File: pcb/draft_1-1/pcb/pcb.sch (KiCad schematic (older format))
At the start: 24 parts, among them J1 USB4110-GF-A, U1 H3LIS200DLTR, U2 ATSAML21J16B-AUT, U3 BQ25155

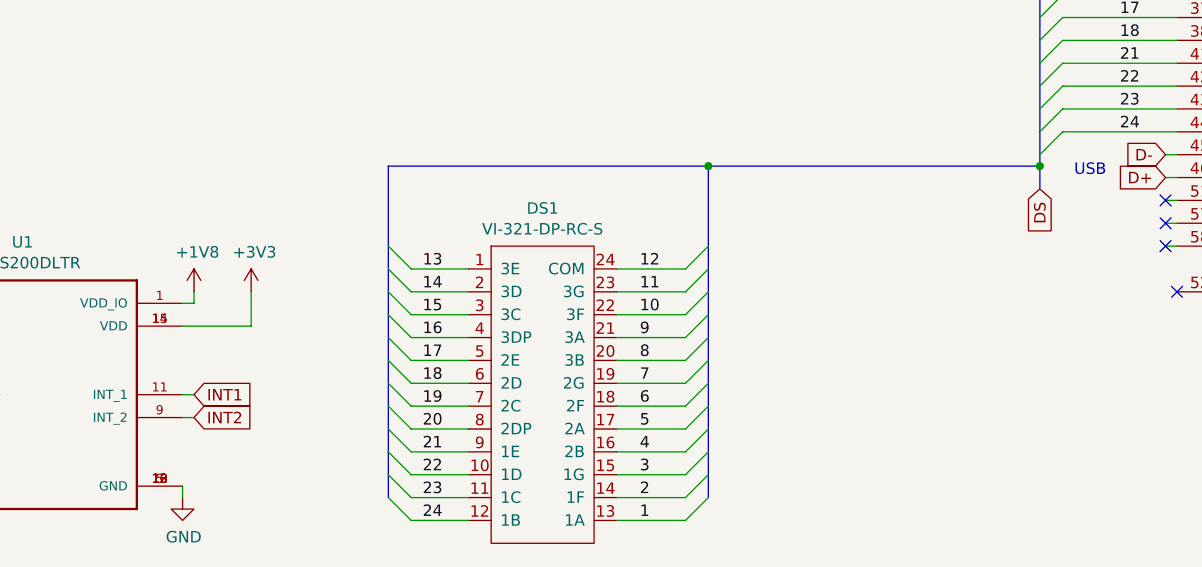
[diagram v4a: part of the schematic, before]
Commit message: added accel decouple caps
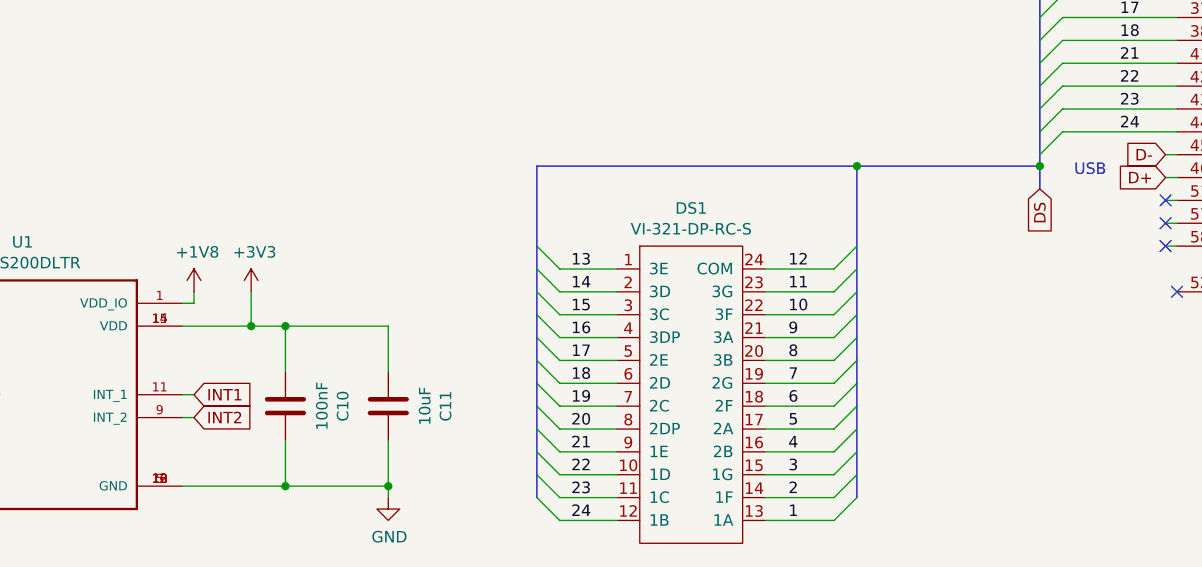
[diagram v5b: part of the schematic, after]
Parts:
- added C10: 100nF, Capacitor_SMD:C_0402_1005Metric, symbol Device:C
- added C11: 10uF, Capacitor_SMD:C_0805_2012Metric, symbol Device:C
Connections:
- net +1V8: now also C10.2, C11.2
- net GND: now also C10.1, C11.1
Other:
- moved on the sheet: DS1
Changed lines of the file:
@@
 $EndComp
 Entry Wire Line
-	4350 5300 4450 5400
-Text Label 4500 5400 0    50   ~ 0
+	5000 5300 5100 5400
+Text Label 5150 5400 0    50   ~ 0
 13
 Entry Wire Line
-	4350 5400 4450 5500
-Entry Wire Line
-	4350 5500 4450 5600
-Entry Wire Line
-	4350 5600 4450 5700
-Entry Wire Line
-	4350 5700 4450 5800
-Entry Wire Line
-	4350 5800 4450 5900
-Entry Wire Line
-	4350 6000 4450 6100
-Entry Wire Line
-	4350 5900 4450 6000
-Entry Wire Line
-	4350 6100 4450 6200
-Entry Wire Line
-	4350 6200 4450 6300
-Entry Wire Line
-	4350 6300 4450 6400
-Entry Wire Line
-	4350 6400 4450 6500
-Text Label 4500 5500 0    50   ~ 0
+	5000 5400 5100 5500
+Entry Wire Line
+	5000 5500 5100 5600
+Entry Wire Line
+	5000 5600 5100 5700
+Entry Wire Line
+	5000 5700 5100 5800
+Entry Wire Line
+	5000 5800 5100 5900
+Entry Wire Line
+	5000 6000 5100 6100
+Entry Wire Line
+	5000 5900 5100 6000
+Entry Wire Line
+	5000 6100 5100 6200
+Entry Wire Line
+	5000 6200 5100 6300
+Entry Wire Line
+	5000 6300 5100 6400
+Entry Wire Line
+	5000 6400 5100 6500
+Text Label 5150 5500 0    50   ~ 0
 14
-Text Label 4500 5600 0    50   ~ 0
+Text Label 5150 5600 0    50   ~ 0
 15
-Text Label 4500 5700 0    50   ~ 0
+Text Label 5150 5700 0    50   ~ 0
 16
-Text Label 4500 5800 0    50   ~ 0
+Text Label 5150 5800 0    50   ~ 0
 17
-Text Label 4500 5900 0    50   ~ 0
+Text Label 5150 5900 0    50   ~ 0
 18
-Text Label 4500 6000 0    50   ~ 0
+Text Label 5150 6000 0    50   ~ 0
 19
-Text Label 4500 6100 0    50   ~ 0
+Text Label 5150 6100 0    50   ~ 0
 20
-Text Label 4500 6200 0    50   ~ 0
+Text Label 5150 6200 0    50   ~ 0
 21
-Text Label 4500 6300 0    50   ~ 0
+Text Label 5150 6300 0    50   ~ 0
 22
-Text Label 4500 6400 0    50   ~ 0
+Text Label 5150 6400 0    50   ~ 0
 23
-Text Label 4500 6500 0    50   ~ 0
+Text Label 5150 6500 0    50   ~ 0
 24
 Entry Wire Line
-	5650 5400 5750 5300
-Entry Wire Line
-	5650 5500 5750 5400
-Entry Wire Line
-	5650 5600 5750 5500
-Entry Wire Line
-	5650 5700 5750 5600
-Entry Wire Line
-	5650 5800 5750 5700
-Entry Wire Line
-	5650 5900 5750 5800
-Entry Wire Line
-	5650 6000 5750 5900
-Entry Wire Line
-	5650 6100 5750 6000
-Entry Wire Line
-	5650 6200 5750 6100
-Entry Wire Line
-	5650 6300 5750 6200
-Entry Wire Line
-	5650 6400 5750 6300
-Entry Wire Line
-	5650 6500 5750 6400
-Text Label 5450 5400 0    50   ~ 0
+	6300 5400 6400 5300
+Entry Wire Line
+	6300 5500 6400 5400
+Entry Wire Line
+	6300 5600 6400 5500
+Entry Wire Line
+	6300 5700 6400 5600
+Entry Wire Line
+	6300 5800 6400 5700
+Entry Wire Line
+	6300 5900 6400 5800
+Entry Wire Line
+	6300 6000 6400 5900
+Entry Wire Line
+	6300 6100 6400 6000
+Entry Wire Line
+	6300 6200 6400 6100
+Entry Wire Line
+	6300 6300 6400 6200
+Entry Wire Line
+	6300 6400 6400 6300
+Entry Wire Line
+	6300 6500 6400 6400
+Text Label 6100 5400 0    50   ~ 0
 12
-Text Label 5450 5500 0    50   ~ 0
+Text Label 6100 5500 0    50   ~ 0
 11
-Text Label 5450 5600 0    50   ~ 0
+Text Label 6100 5600 0    50   ~ 0
 10
-Text Label 5450 5700 0    50   ~ 0
+Text Label 6100 5700 0    50   ~ 0
 9
-Text Label 5450 5800 0    50   ~ 0
+Text Label 6100 5800 0    50   ~ 0
 8
-Text Label 5450 5900 0    50   ~ 0
+Text Label 6100 5900 0    50   ~ 0
 7
-Text Label 5450 6000 0    50   ~ 0
+Text Label 6100 6000 0    50   ~ 0
 6
-Text Label 5450 6100 0    50   ~ 0
+Text Label 6100 6100 0    50   ~ 0
 5
-Text Label 5450 6200 0    50   ~ 0
+Text Label 6100 6200 0    50   ~ 0
 4
-Text Label 5450 6300 0    50   ~ 0
+Text Label 6100 6300 0    50   ~ 0
 3
-Text Label 5450 6400 0    50   ~ 0
+Text Label 6100 6400 0    50   ~ 0
 2
-Text Label 5450 6500 0    50   ~ 0
+Text Label 6100 6500 0    50   ~ 0
 1
 Text GLabel 1150 5950 0    50   Input ~ 0
@@
 L power:GND #PWR0102
 U 1 1 5E0D1684
-P 3450 6400
-F 0 "#PWR0102" H 3450 6150 50  0001 C CNN
-F 1 "GND" H 3455 6227 50  0000 C CNN
-F 2 "" H 3450 6400 50  0001 C CNN
-F 3 "" H 3450 6400 50  0001 C CNN
-	1    3450 6400
-	1    0    0    -1
-$EndComp
-Wire Wire Line
-	3450 6350 3450 6400
+P 4350 6400
+F 0 "#PWR0102" H 4350 6150 50  0001 C CNN
+F 1 "GND" H 4355 6227 50  0000 C CNN
+F 2 "" H 4350 6400 50  0001 C CNN
+F 3 "" H 4350 6400 50  0001 C CNN
+	1    4350 6400
+	1    0    0    -1
+$EndComp
 $Comp
 L power:+1V8 #PWR0103
@@
 	1    0    0    -1
 $EndComp
-Text GLabel 3500 5950 2    50   Input ~ 0
-INT1
 Text GLabel 3500 6050 2    50   Input ~ 0
 INT2
@@
 L Custom:VI-321-DP-RC-S DS1
 U 1 1 5E20A245
-P 5050 5950
-F 0 "DS1" H 5025 6765 50  0000 C CNN
-F 1 "VI-321-DP-RC-S" H 5025 6674 50  0000 C CNN
-F 2 "custom:VI-321-DP-RC-S" H 5250 6350 50  0001 C CNN
-F 3 "" H 5250 6350 50  0001 C CNN
-	1    5050 5950
+P 5700 5950
+F 0 "DS1" H 5675 6765 50  0000 C CNN
+F 1 "VI-321-DP-RC-S" H 5675 6674 50  0000 C CNN
+F 2 "custom:VI-321-DP-RC-S" H 5900 6350 50  0001 C CNN
+F 3 "" H 5900 6350 50  0001 C CNN
+	1    5700 5950
 	1    0    0    -1
 $EndComp
@@
 	7300 4800 7800 4800
 Wire Wire Line
-	5350 5400 5650 5400
-Wire Wire Line
-	5350 5500 5650 5500
-Wire Wire Line
-	5350 5600 5650 5600
-Wire Wire Line
-	5350 5700 5650 5700
-Wire Wire Line
-	5350 5800 5650 5800
-Wire Wire Line
-	5350 5900 5650 5900
-Wire Wire Line
-	5350 6000 5650 6000
-Wire Wire Line
-	5350 6100 5650 6100
-Wire Wire Line
-	5350 6200 5650 6200
-Wire Wire Line
-	5350 6300 5650 6300
-Wire Wire Line
-	5350 6400 5650 6400
-Wire Wire Line
-	5350 6500 5650 6500
-Wire Wire Line
-	4450 5400 4700 5400
-Wire Wire Line
-	4450 5500 4700 5500
-Wire Wire Line
-	4450 5600 4700 5600
-Wire Wire Line
-	4450 5700 4700 5700
-Wire Wire Line
-	4450 5800 4700 5800
-Wire Wire Line
-	4450 5900 4700 5900
-Wire Wire Line
-	4450 6000 4700 6000
-Wire Wire Line
-	4450 6100 4700 6100
-Wire Wire Line
-	4450 6200 4700 6200
-Wire Wire Line
-	4450 6300 4700 6300
-Wire Wire Line
-	4450 6400 4700 6400
-Wire Wire Line
-	4450 6500 4700 6500
+	6000 5400 6300 5400
+Wire Wire Line
+	6000 5500 6300 5500
+Wire Wire Line
+	6000 5600 6300 5600
+Wire Wire Line
+	6000 5700 6300 5700
+Wire Wire Line
+	6000 5800 6300 5800
+Wire Wire Line
+	6000 5900 6300 5900
+Wire Wire Line
+	6000 6000 6300 6000
+Wire Wire Line
+	6000 6100 6300 6100
+Wire Wire Line
+	6000 6200 6300 6200
+Wire Wire Line
+	6000 6300 6300 6300
+Wire Wire Line
+	6000 6400 6300 6400
+Wire Wire Line
+	6000 6500 6300 6500
+Wire Wire Line
+	5100 5400 5350 5400
+Wire Wire Line
+	5100 5500 5350 5500
+Wire Wire Line
+	5100 5600 5350 5600
+Wire Wire Line
+	5100 5700 5350 5700
+Wire Wire Line
+	5100 5800 5350 5800
+Wire Wire Line
+	5100 5900 5350 5900
+Wire Wire Line
+	5100 6000 5350 6000
+Wire Wire Line
+	5100 6100 5350 6100
+Wire Wire Line
+	5100 6200 5350 6200
+Wire Wire Line
+	5100 6300 5350 6300
+Wire Wire Line
+	5100 6400 5350 6400
+Wire Wire Line
+	5100 6500 5350 6500
 Wire Bus Line
-	4350 4950 5750 4950
-Connection ~ 5750 4950
-Wire Bus Line
-	5750 4950 7200 4950
+	5000 4950 6400 4950
 Text GLabel 7200 5050 3    50   Input ~ 0
 DS
@@
 Text Label 7550 4500 0    50   ~ 0
 21
-Wire Bus Line
-	7200 5050 7200 4950
-Connection ~ 7200 4950
 Wire Wire Line
 	7500 3000 7800 3000
@@
 NoConn ~ 7750 5300
 NoConn ~ 7800 5500
-Wire Bus Line
-	10200 3700 10200 4500
-Wire Bus Line
-	4350 4950 4350 6400
-Wire Bus Line
-	5750 4950 5750 6400
-Wire Bus Line
-	7200 3400 7200 4950
 Text Label 7550 4400 0    50   ~ 0
 18
 Text Label 7550 4300 0    50   ~ 0
 17
+Wire Bus Line
+	6400 4950 7200 4950
+Connection ~ 6400 4950
+Connection ~ 7200 4950
+Wire Bus Line
+	7200 4950 7200 5050
+Wire Wire Line
+	3750 5650 3900 5650
+Connection ~ 3750 5650
+Wire Wire Line
+	3900 5650 4350 5650
+Connection ~ 3900 5650
+Wire Wire Line
+	3450 6350 3900 6350
+Wire Wire Line
+	4350 6350 4350 6400
+Connection ~ 4350 6350
+Connection ~ 3900 6350
+Wire Wire Line
+	3900 6350 4350 6350
+$Comp
+L Device:C C10
+U 1 1 5E17A014
+P 3900 6000
+F 0 "C10" V 3648 6000 50  0000 C CNN
+F 1 "100nF" V 3739 6000 50  0000 C CNN
+F 2 "Capacitor_SMD:C_0402_1005Metric" H 3938 5850 50  0001 C CNN
+F 3 "~" H 3900 6000 50  0001 C CNN
+	1    3900 6000
+	-1   0    0    1
+$EndComp
+$Comp
+L Device:C C11
+U 1 1 5E16FE35
+P 4350 6000
+F 0 "C11" V 4098 6000 50  0000 C CNN
+F 1 "10uF" V 4189 6000 50  0000 C CNN
+F 2 "Capacitor_SMD:C_0805_2012Metric" H 4388 5850 50  0001 C CNN
+F 3 "~" H 4350 6000 50  0001 C CNN
+	1    4350 6000
+	-1   0    0    1
+$EndComp
+Text GLabel 3500 5950 2    50   Input ~ 0
+INT1
+Wire Wire Line
+	3900 6150 3900 6350
+Wire Wire Line
+	4350 6150 4350 6350
+Wire Wire Line
+	3900 5650 3900 5850
+Wire Wire Line
+	4350 5650 4350 5850
+Wire Bus Line
+	10200 3700 10200 4500
+Wire Bus Line
+	5000 4950 5000 6400
+Wire Bus Line
+	6400 4950 6400 6400
+Wire Bus Line
+	7200 3400 7200 4950
 $EndSCHEMATC

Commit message: candidate layout done
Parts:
- C11: value 10uF -> 22uF
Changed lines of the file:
@@
 P 4350 6000
 F 0 "C11" V 4098 6000 50  0000 C CNN
-F 1 "10uF" V 4189 6000 50  0000 C CNN
+F 1 "22uF" V 4189 6000 50  0000 C CNN
 F 2 "Capacitor_SMD:C_0805_2012Metric" H 4388 5850 50  0001 C CNN
 F 3 "~" H 4350 6000 50  0001 C CNN

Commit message: as built
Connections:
- net 1 renamed 1A
- net 10 renamed 3F
- net 11 renamed 3G
- net 12 renamed COM
- net 13 renamed 3E
- net 14 renamed 3D
- net 15 renamed 3C
- net 16 renamed 3DP
- net 17 renamed 2E
- net 18 renamed 2D
- net 19 renamed 2C
- net 2 renamed 1F
- net 20 renamed 2DP
- net 21 renamed 1E
- net 22 renamed 1D
- net 23 renamed 1C
- net 24 renamed 1B
- net 3 renamed 1G
- net 4 renamed 2B
- net 5 renamed 2A
- net 6 renamed 2F
- net 7 renamed 2G
- net 8 renamed 3B
- net 9 renamed 3A
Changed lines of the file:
@@
 	5000 5300 5100 5400
 Text Label 5150 5400 0    50   ~ 0
-13
+3E
 Entry Wire Line
 	5000 5400 5100 5500
@@
 	5000 6400 5100 6500
 Text Label 5150 5500 0    50   ~ 0
-14
+3D
 Text Label 5150 5600 0    50   ~ 0
-15
+3C
 Text Label 5150 5700 0    50   ~ 0
-16
+3DP
 Text Label 5150 5800 0    50   ~ 0
-17
-Text Label 5150 5900 0    50   ~ 0
-18
+2E
 Text Label 5150 6000 0    50   ~ 0
-19
+2C
 Text Label 5150 6100 0    50   ~ 0
-20
+2DP
 Text Label 5150 6200 0    50   ~ 0
-21
+1E
 Text Label 5150 6300 0    50   ~ 0
-22
+1D
 Text Label 5150 6400 0    50   ~ 0
-23
+1C
 Text Label 5150 6500 0    50   ~ 0
-24
+1B
 Entry Wire Line
 	6300 5400 6400 5300
@@
 Entry Wire Line
 	6300 6500 6400 6400
-Text Label 6100 5400 0    50   ~ 0
-12
 Text Label 6100 5500 0    50   ~ 0
-11
+3G
 Text Label 6100 5600 0    50   ~ 0
-10
+3F
 Text Label 6100 5700 0    50   ~ 0
-9
+3A
 Text Label 6100 5800 0    50   ~ 0
-8
+3B
 Text Label 6100 5900 0    50   ~ 0
-7
+2G
 Text Label 6100 6000 0    50   ~ 0
-6
+2F
 Text Label 6100 6100 0    50   ~ 0
-5
+2A
 Text Label 6100 6200 0    50   ~ 0
-4
+2B
 Text Label 6100 6300 0    50   ~ 0
-3
+1G
 Text Label 6100 6400 0    50   ~ 0
-2
+1F
 Text Label 6100 6500 0    50   ~ 0
-1
+1A
 Text GLabel 1150 5950 0    50   Input ~ 0
 SDA
@@
 	7750 5300 7800 5300
 Text Label 7550 3300 0    50   ~ 0
-1
+1A
 Text Notes 6850 3050 0    50   ~ 0
 EXTINT[5]
@@
 DS
 Text Label 9900 3900 0    50   ~ 0
-5
+2A
 Wire Wire Line
 	10100 3900 9800 3900
@@
 	8700 5900 8900 5900
 Connection ~ 8900 5900
-$Comp
-L MCU_Microchip_SAML:ATSAML21J16B-AUT U2
-U 1 1 5E306B11
-P 8800 4000
-F 0 "U2" H 8800 2011 50  0000 C CNN
-F 1 "ATSAML21J16B-AUT" H 8800 1920 50  0000 C CNN
-F 2 "Package_QFP:TQFP-64_10x10mm_P0.5mm" H 10000 5800 50  0001 C CNN
-F 3 "http://ww1.microchip.com/downloads/en/DeviceDoc/60001477A.pdf" H 8800 4000 50  0001 C CNN
-	1    8800 4000
-	1    0    0    -1
-$EndComp
 Wire Wire Line
 	6200 2350 6250 2350
@@
 NoConn ~ 9800 4800
 Text Label 7550 3400 0    50   ~ 0
-2
+1F
 Text Label 7550 3500 0    50   ~ 0
-3
+1G
 Text Label 7550 3600 0    50   ~ 0
-4
+2B
 Text Label 7550 3700 0    50   ~ 0
-11
+3G
 Text Label 7550 3800 0    50   ~ 0
-12
+COM
 Text Label 7550 3900 0    50   ~ 0
-13
+3E
 Text Label 7550 4000 0    50   ~ 0
-14
+3D
 Text Label 7550 4100 0    50   ~ 0
-15
-Text Label 7550 4200 0    50   ~ 0
-16
+3C
 Text Label 9900 4000 0    50   ~ 0
-6
+2F
 Text Label 9900 4100 0    50   ~ 0
-7
+2G
 Text Label 9900 4200 0    50   ~ 0
-8
-Text Label 9900 4300 0    50   ~ 0
-9
+3B
 Text Label 9900 4400 0    50   ~ 0
-10
+3F
 Text Label 9900 4500 0    50   ~ 0
-19
+2C
 Text Label 9900 4600 0    50   ~ 0
-20
+2DP
 Text Label 7550 4800 0    50   ~ 0
-24
+1B
 Text Label 7550 4700 0    50   ~ 0
-23
+1C
 Text Label 7550 4600 0    50   ~ 0
-22
+1D
 Text Label 7550 4500 0    50   ~ 0
-21
+1E
 Wire Wire Line
 	7500 3000 7800 3000
@@
 NoConn ~ 7750 5300
 NoConn ~ 7800 5500
-Text Label 7550 4400 0    50   ~ 0
-18
 Text Label 7550 4300 0    50   ~ 0
-17
+2E
 Wire Bus Line
 	6400 4950 7200 4950
@@
 Wire Bus Line
 	7200 3400 7200 4950
+Text Label 5150 5900 0    50   ~ 0
+2D
+Text Label 7550 4200 0    50   ~ 0
+3DP
+Text Label 7550 4400 0    50   ~ 0
+2D
+$Comp
+L MCU_Microchip_SAML:ATSAML21J16B-AUT U2
+U 1 1 5E306B11
+P 8800 4000
+F 0 "U2" H 8800 2011 50  0000 C CNN
+F 1 "ATSAML21J16B-AUT" H 8800 1920 50  0000 C CNN
+F 2 "Package_QFP:TQFP-64_10x10mm_P0.5mm" H 10000 5800 50  0001 C CNN
+F 3 "http://ww1.microchip.com/downloads/en/DeviceDoc/60001477A.pdf" H 8800 4000 50  0001 C CNN
+	1    8800 4000
+	1    0    0    -1
+$EndComp
+Text Label 6100 5400 0    50   ~ 0
+COM
+Text Label 9900 4300 0    50   ~ 0
+3A
 $EndSCHEMATC
